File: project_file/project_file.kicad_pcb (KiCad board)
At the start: 2 copper layers, 44 x 84 mm, 76 parts, among them IC1 BMI055, J1 Power Module 1, J10 CAP & ADC IN, J11 SPI Port, J12 I2C A, J13 FMU PWM OUT, J14 PPM RC, J15 2908-05WB-MG, J16 RC, J17 SBUS, J18 IO/PWM out, J2 Power Module 2, J3 USB, J4 Telemetry 1, J5 Telemetry 2, J6 UART & I2C B, J7 CAN 1, J8 CAN 2, J9 GPS Module, U1 STM32F765IIKx, U10 TJA1051TK-3, U11 LT3080xDD, U12 LP5907MFX-3.3, U13 LP5907MFX-3.3, U3 IST8310, U4 ICM-20602, U5 ICM-20689, U6 MS5611-01BA, U8 STM32F103V8Tx, U9 TJA1051TK-3, Y1 ABM2-8.000MHZ-D4Y-T

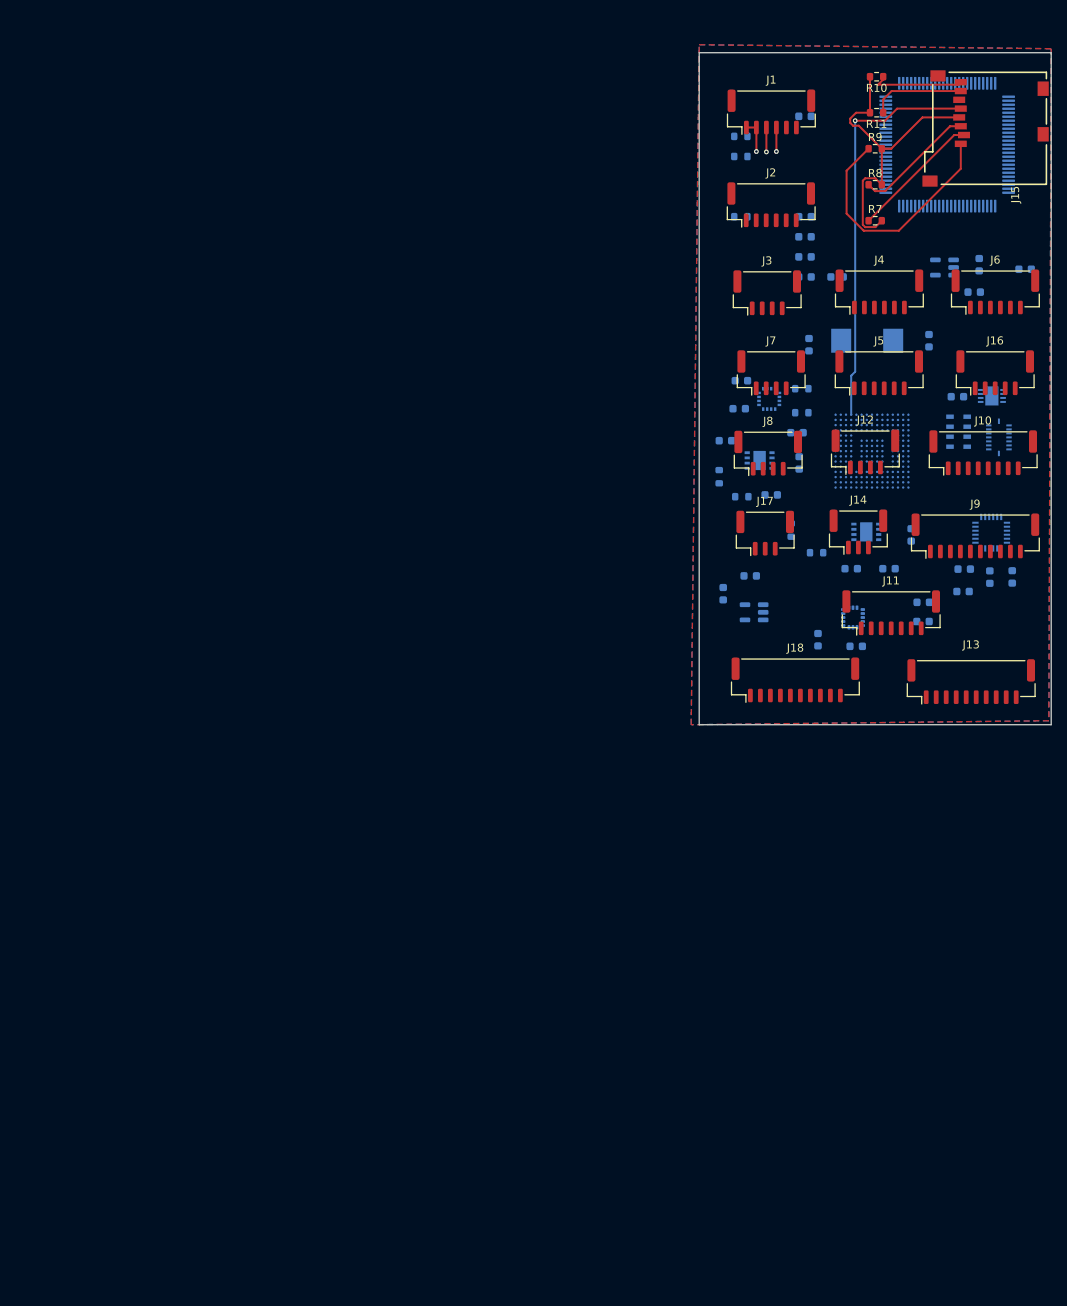
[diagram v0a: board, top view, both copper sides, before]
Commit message: CAN JST to pads, group pcb components tgt
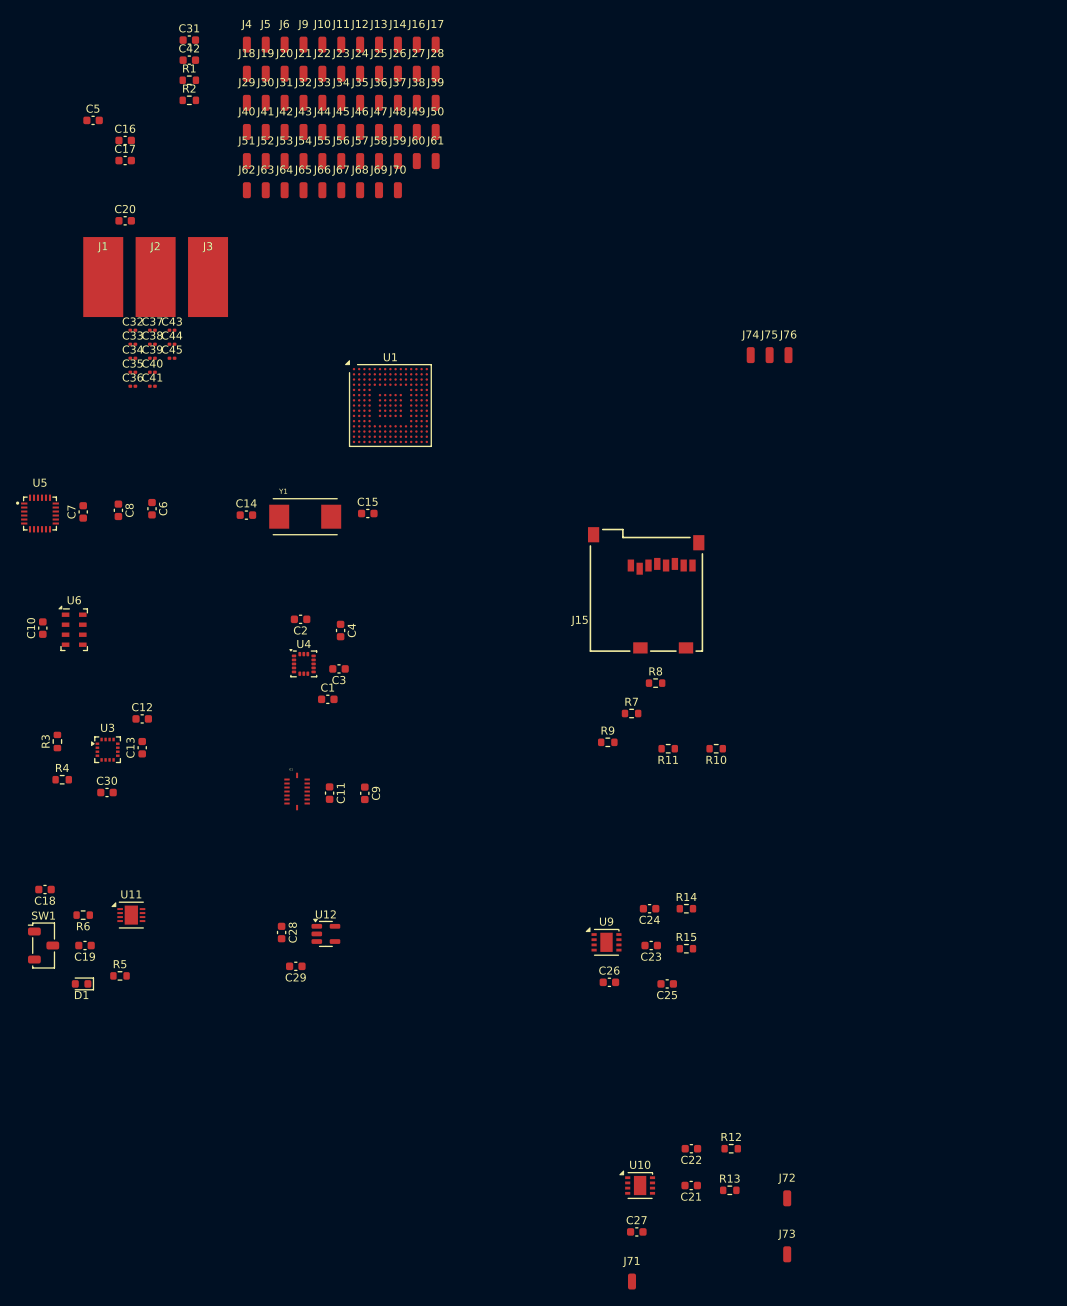
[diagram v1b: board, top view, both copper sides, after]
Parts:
- removed J7: CAN 1, Connector_JST:JST_GH_BM04B-GHS-TBT_1x04-1MP_P1.25mm_Vertical
- removed J8: CAN 2, Connector_JST:JST_GH_BM04B-GHS-TBT_1x04-1MP_P1.25mm_Vertical
- removed U13: LP5907MFX-3.3, Package_TO_SOT_SMD:SOT-23-5
- removed U8: STM32F103V8Tx, Package_QFP:LQFP-100_14x14mm_P0.5mm
- added C32: 100nf, Capacitor_SMD:C_0201_0603Metric, F.Cu at (36.2, 64.7)
- added C33: 100nf, Capacitor_SMD:C_0201_0603Metric, F.Cu at (36.2, 66.4)
- added C34: 100nf, Capacitor_SMD:C_0201_0603Metric, F.Cu at (36.2, 68.2)
- added C35: 100nf, Capacitor_SMD:C_0201_0603Metric, F.Cu at (36.2, 69.9)
- added C36: 100nf, Capacitor_SMD:C_0201_0603Metric, F.Cu at (36.2, 71.7)
- added C37: 100nf, Capacitor_SMD:C_0201_0603Metric, F.Cu at (38.7, 64.7)
- added C38: 100nf, Capacitor_SMD:C_0201_0603Metric, F.Cu at (38.7, 66.4)
- added C39: 100nf, Capacitor_SMD:C_0201_0603Metric, F.Cu at (38.7, 68.2)
- added C40: 100nf, Capacitor_SMD:C_0201_0603Metric, F.Cu at (38.7, 69.9)
- added C41: 100nf, Capacitor_SMD:C_0201_0603Metric, F.Cu at (38.7, 71.7)
- added C42: 0.1uF, Capacitor_SMD:C_0603_1608Metric, F.Cu at (43.3, 30.9)
- added C43: 100nf, Capacitor_SMD:C_0201_0603Metric, F.Cu at (41.1, 64.7)
- added C44: 100nf, Capacitor_SMD:C_0201_0603Metric, F.Cu at (41.1, 66.4)
- added C45: 100nf, Capacitor_SMD:C_0201_0603Metric, F.Cu at (41.1, 68.2)
- added D1: LED, LED_SMD:LED_0603_1608Metric, F.Cu at (29.8, 146.4)
- added J19: Conn_01x01_Socket, Connector_Wire:SolderWirePad_1x01_SMD_1x2mm, F.Cu at (52.8, 32.6)
- added J20: Conn_01x01_Socket, Connector_Wire:SolderWirePad_1x01_SMD_1x2mm, F.Cu at (55.2, 32.6)
- added J21: Conn_01x01_Socket, Connector_Wire:SolderWirePad_1x01_SMD_1x2mm, F.Cu at (57.5, 32.6)
- added J22: Conn_01x01_Socket, Connector_Wire:SolderWirePad_1x01_SMD_1x2mm, F.Cu at (59.9, 32.6)
- added J23: Conn_01x01_Socket, Connector_Wire:SolderWirePad_1x01_SMD_1x2mm, F.Cu at (62.3, 32.6)
- added J24: Conn_01x01_Socket, Connector_Wire:SolderWirePad_1x01_SMD_1x2mm, F.Cu at (64.6, 32.6)
- added J25: Conn_01x01_Socket, Connector_Wire:SolderWirePad_1x01_SMD_1x2mm, F.Cu at (67.0, 32.6)
- added J26: Conn_01x01_Socket, Connector_Wire:SolderWirePad_1x01_SMD_1x2mm, F.Cu at (69.3, 32.6)
- added J27: Conn_01x01_Socket, Connector_Wire:SolderWirePad_1x01_SMD_1x2mm, F.Cu at (71.7, 32.6)
- added J28: Conn_01x01_Socket, Connector_Wire:SolderWirePad_1x01_SMD_1x2mm, F.Cu at (74.1, 32.6)
- added J29: Conn_01x01_Socket, Connector_Wire:SolderWirePad_1x01_SMD_1x2mm, F.Cu at (50.5, 36.3)
- added J30: Conn_01x01_Socket, Connector_Wire:SolderWirePad_1x01_SMD_1x2mm, F.Cu at (52.8, 36.3)
- added J31: Conn_01x01_Socket, Connector_Wire:SolderWirePad_1x01_SMD_1x2mm, F.Cu at (55.2, 36.3)
- added J32: Conn_01x01_Socket, Connector_Wire:SolderWirePad_1x01_SMD_1x2mm, F.Cu at (57.5, 36.3)
- added J33: Conn_01x01_Socket, Connector_Wire:SolderWirePad_1x01_SMD_1x2mm, F.Cu at (59.9, 36.3)
- added J34: Conn_01x01_Socket, Connector_Wire:SolderWirePad_1x01_SMD_1x2mm, F.Cu at (62.3, 36.3)
- added J35: Conn_01x01_Socket, Connector_Wire:SolderWirePad_1x01_SMD_1x2mm, F.Cu at (64.6, 36.3)
- added J36: Conn_01x01_Socket, Connector_Wire:SolderWirePad_1x01_SMD_1x2mm, F.Cu at (67.0, 36.3)
- added J37: Conn_01x01_Socket, Connector_Wire:SolderWirePad_1x01_SMD_1x2mm, F.Cu at (69.3, 36.3)
- added J38: Conn_01x01_Socket, Connector_Wire:SolderWirePad_1x01_SMD_1x2mm, F.Cu at (71.7, 36.3)
- added J39: Conn_01x01_Socket, Connector_Wire:SolderWirePad_1x01_SMD_1x2mm, F.Cu at (74.1, 36.3)
- added J40: Conn_01x01_Socket, Connector_Wire:SolderWirePad_1x01_SMD_1x2mm, F.Cu at (50.5, 39.9)
- added J41: Conn_01x01_Socket, Connector_Wire:SolderWirePad_1x01_SMD_1x2mm, F.Cu at (52.8, 39.9)
- added J42: Conn_01x01_Socket, Connector_Wire:SolderWirePad_1x01_SMD_1x2mm, F.Cu at (55.2, 39.9)
- added J43: Conn_01x01_Socket, Connector_Wire:SolderWirePad_1x01_SMD_1x2mm, F.Cu at (57.5, 39.9)
- added J44: Conn_01x01_Socket, Connector_Wire:SolderWirePad_1x01_SMD_1x2mm, F.Cu at (59.9, 39.9)
- added J45: Conn_01x01_Socket, Connector_Wire:SolderWirePad_1x01_SMD_1x2mm, F.Cu at (62.3, 39.9)
- added J46: Conn_01x01_Socket, Connector_Wire:SolderWirePad_1x01_SMD_1x2mm, F.Cu at (64.6, 39.9)
- added J47: Conn_01x01_Socket, Connector_Wire:SolderWirePad_1x01_SMD_1x2mm, F.Cu at (67.0, 39.9)
- added J48: Conn_01x01_Socket, Connector_Wire:SolderWirePad_1x01_SMD_1x2mm, F.Cu at (69.3, 39.9)
- added J49: Conn_01x01_Socket, Connector_Wire:SolderWirePad_1x01_SMD_1x2mm, F.Cu at (71.7, 39.9)
- added J50: Conn_01x01_Socket, Connector_Wire:SolderWirePad_1x01_SMD_1x2mm, F.Cu at (74.1, 39.9)
- added J51: Conn_01x01_Socket, Connector_Wire:SolderWirePad_1x01_SMD_1x2mm, F.Cu at (50.5, 43.5)
- added J52: Conn_01x01_Socket, Connector_Wire:SolderWirePad_1x01_SMD_1x2mm, F.Cu at (52.8, 43.5)
- added J53: Conn_01x01_Socket, Connector_Wire:SolderWirePad_1x01_SMD_1x2mm, F.Cu at (55.2, 43.5)
- added J54: Conn_01x01_Socket, Connector_Wire:SolderWirePad_1x01_SMD_1x2mm, F.Cu at (57.5, 43.5)
- added J55: Conn_01x01_Socket, Connector_Wire:SolderWirePad_1x01_SMD_1x2mm, F.Cu at (59.9, 43.5)
- added J56: Conn_01x01_Socket, Connector_Wire:SolderWirePad_1x01_SMD_1x2mm, F.Cu at (62.3, 43.5)
- added J57: Conn_01x01_Socket, Connector_Wire:SolderWirePad_1x01_SMD_1x2mm, F.Cu at (64.6, 43.5)
- added J58: Conn_01x01_Socket, Connector_Wire:SolderWirePad_1x01_SMD_1x2mm, F.Cu at (67.0, 43.5)
- added J59: Conn_01x01_Socket, Connector_Wire:SolderWirePad_1x01_SMD_1x2mm, F.Cu at (69.3, 43.5)
- added J60: Conn_01x01_Socket, Connector_Wire:SolderWirePad_1x01_SMD_1x2mm, F.Cu at (71.7, 43.5)
- added J61: Conn_01x01_Socket, Connector_Wire:SolderWirePad_1x01_SMD_1x2mm, F.Cu at (74.1, 43.5)
- added J62: Conn_01x01_Socket, Connector_Wire:SolderWirePad_1x01_SMD_1x2mm, F.Cu at (50.5, 47.2)
- added J63: Conn_01x01_Socket, Connector_Wire:SolderWirePad_1x01_SMD_1x2mm, F.Cu at (52.8, 47.2)
- added J64: Conn_01x01_Socket, Connector_Wire:SolderWirePad_1x01_SMD_1x2mm, F.Cu at (55.2, 47.2)
- added J65: Conn_01x01_Socket, Connector_Wire:SolderWirePad_1x01_SMD_1x2mm, F.Cu at (57.5, 47.2)
- added J66: Conn_01x01_Socket, Connector_Wire:SolderWirePad_1x01_SMD_1x2mm, F.Cu at (59.9, 47.2)
- added J67: Conn_01x01_Socket, Connector_Wire:SolderWirePad_1x01_SMD_1x2mm, F.Cu at (62.3, 47.2)
- added J68: Conn_01x01_Socket, Connector_Wire:SolderWirePad_1x01_SMD_1x2mm, F.Cu at (64.6, 47.2)
- added J69: Conn_01x01_Socket, Connector_Wire:SolderWirePad_1x01_SMD_1x2mm, F.Cu at (67.0, 47.2)
- added J70: Conn_01x01_Socket, Connector_Wire:SolderWirePad_1x01_SMD_1x2mm, F.Cu at (69.3, 47.2)
- added J71: Conn_01x01_Socket, Connector_Wire:SolderWirePad_1x01_SMD_1x2mm, F.Cu at (98.6, 183.6)
- added J72: Conn_01x01_Socket, Connector_Wire:SolderWirePad_1x01_SMD_1x2mm, F.Cu at (118.0, 173.2)
- added J73: Conn_01x01_Socket, Connector_Wire:SolderWirePad_1x01_SMD_1x2mm, F.Cu at (118.0, 180.2)
- added J74: Conn_01x01_Socket, Connector_Wire:SolderWirePad_1x01_SMD_1x2mm, F.Cu at (113.4, 67.8)
- added J75: Conn_01x01_Socket, Connector_Wire:SolderWirePad_1x01_SMD_1x2mm, F.Cu at (115.8, 67.8)
- added J76: Conn_01x01_Socket, Connector_Wire:SolderWirePad_1x01_SMD_1x2mm, F.Cu at (118.2, 67.8)
- added R5: 300, Resistor_SMD:R_0603_1608Metric, F.Cu at (34.6, 145.4)
- added SW1: SW_Nidec_CAS-120A1, Button_Switch_SMD:Nidec_Copal_CAS-120A, F.Cu at (25.1, 141.6)
- C1, C10, C11, C12, C13, C14, C15, C16, C17, C18, C19, C2, C20, C21, C22, C23, C24, C25, C26, C27, C28, C29, C3, C4, C6, C7, C8, C9, IC1, R1, R12, R13, R14, R15, R2, R3, R4, R6, U1, U10, U11, U12, U3, U4, U5, U6, U9, Y1: moved to F.Cu
- C30, C31: value 1uf -> 0.1uF; moved to F.Cu
- C5: value 0.47uF -> 0.1uF; moved to F.Cu
- J1: value Power Module 1 -> Conn_01x01_Socket; footprint Connector_JST:JST_GH_BM06B-GHS-TBT_1x06-1MP_P1.25mm_Vertical -> Connector_Wire:SolderWirePad_1x01_SMD_5x10mm
- J10: value CAP & ADC IN -> Conn_01x01_Socket; footprint Connector_JST:JST_GH_BM08B-GHS-TBT_1x08-1MP_P1.25mm_Vertical -> Connector_Wire:SolderWirePad_1x01_SMD_1x2mm
- J11: value SPI Port -> Conn_01x01_Socket; footprint Connector_JST:JST_GH_BM07B-GHS-TBT_1x07-1MP_P1.25mm_Vertical -> Connector_Wire:SolderWirePad_1x01_SMD_1x2mm
- J12: value I2C A -> Conn_01x01_Socket; footprint Connector_JST:JST_GH_BM04B-GHS-TBT_1x04-1MP_P1.25mm_Vertical -> Connector_Wire:SolderWirePad_1x01_SMD_1x2mm
- J13: value FMU PWM OUT -> Conn_01x01_Socket; footprint Connector_JST:JST_EH_B10B-EH-A_1x10_P2.50mm_Vertical -> Connector_Wire:SolderWirePad_1x01_SMD_1x2mm
- J14: value PPM RC -> Conn_01x01_Socket; footprint Connector_JST:JST_GH_BM03B-GHS-TBT_1x03-1MP_P1.25mm_Vertical -> Connector_Wire:SolderWirePad_1x01_SMD_1x2mm
- J16: value RC -> Conn_01x01_Socket; footprint Connector_JST:JST_GH_BM05B-GHS-TBT_1x05-1MP_P1.25mm_Vertical -> Connector_Wire:SolderWirePad_1x01_SMD_1x2mm
- J17: value SBUS -> Conn_01x01_Socket; footprint Connector_JST:JST_GH_BM03B-GHS-TBT_1x03-1MP_P1.25mm_Vertical -> Connector_Wire:SolderWirePad_1x01_SMD_1x2mm
- J18: value IO/PWM out -> Conn_01x01_Socket; footprint Connector_JST:JST_GH_BM10B-GHS-TBT_1x10-1MP_P1.25mm_Vertical -> Connector_Wire:SolderWirePad_1x01_SMD_1x2mm
- J2: value Power Module 2 -> Conn_01x01_Socket; footprint Connector_JST:JST_GH_BM06B-GHS-TBT_1x06-1MP_P1.25mm_Vertical -> Connector_Wire:SolderWirePad_1x01_SMD_5x10mm
- J3: value USB -> Conn_01x01_Socket; footprint Connector_JST:JST_GH_BM04B-GHS-TBT_1x04-1MP_P1.25mm_Vertical -> Connector_Wire:SolderWirePad_1x01_SMD_5x10mm
- J4: value Telemetry 1 -> Conn_01x01_Socket; footprint Connector_JST:JST_GH_BM06B-GHS-TBT_1x06-1MP_P1.25mm_Vertical -> Connector_Wire:SolderWirePad_1x01_SMD_1x2mm
- J5: value Telemetry 2 -> Conn_01x01_Socket; footprint Connector_JST:JST_GH_BM06B-GHS-TBT_1x06-1MP_P1.25mm_Vertical -> Connector_Wire:SolderWirePad_1x01_SMD_1x2mm
- J6: value UART & I2C B -> Conn_01x01_Socket; footprint Connector_JST:JST_GH_BM06B-GHS-TBT_1x06-1MP_P1.25mm_Vertical -> Connector_Wire:SolderWirePad_1x01_SMD_1x2mm
- J9: value GPS Module -> Conn_01x01_Socket; footprint Connector_JST:JST_GH_BM10B-GHS-TBT_1x10-1MP_P1.25mm_Vertical -> Connector_Wire:SolderWirePad_1x01_SMD_1x2mm
- moved C5 125.8 mm to (31.2, 38.5), turned to 0 degrees
- moved U11 125.6 mm to (36.0, 137.8), turned to 0 degrees
- moved C18 123.6 mm to (25.2, 134.6)
- moved C19 122.8 mm to (30.2, 141.6)
- moved C28 120.7 mm to (54.8, 140.0)
- moved R6 119.9 mm to (30.0, 137.8)
- moved C29 119.6 mm to (56.6, 144.2), turned to 180 degrees
- moved U5 118.9 mm to (24.6, 87.6), turned to 0 degrees
- moved C10 117.9 mm to (24.9, 101.9), turned to 90 degrees
- moved C7 116.4 mm to (30.0, 87.4), turned to 90 degrees
- moved U12 113.7 mm to (60.3, 140.2), turned to 0 degrees
- moved U6 113.3 mm to (28.9, 102.1), turned to 0 degrees
- moved J13 108.3 mm to (67.0, 29.0)
- moved C8 106.1 mm to (34.4, 87.2), turned to -90 degrees
- moved J9 104.0 mm to (57.5, 29.0)
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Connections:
- C10 pad 2: VDD_sensors -> VDD_3V3
- C11 pad 1: VDDIO_sensors -> VDD_3V3
- C18 pad 1: BMS_22.2V -> Net-(U11-V_{CONTROL})
- C2 pad 2: VDD_sensors -> VDD_3V3
- C20 pad 1: Net-(J8-Pin_2) -> GND
- C25 pad 1: Net-(J7-Pin_2) -> GND
- C26 pad 2: /VDDIO -> VDD_3V3
- C27 pad 2: /VDDIO -> VDD_3V3
- C3 pad 1: VDDIO_sensors -> VDD_3V3
- C30 pad 1: BMS_22.2V -> VDD_3V3
- C31 pad 1: VCC_5V -> Net-(J31-Pin_1)
- C31 pad 2: GND -> VDD_3V3
- C4 pad 2: VDD_sensors -> VDD_3V3
- C6 pad 2: VDD_sensors -> VDD_3V3
- C7 pad 1: VDDIO_sensors -> VDD_3V3
- C8 pad 2: VDD_sensors -> VDD_3V3
- C9 pad 1: VDD_sensors -> VDD_3V3
- IC1 pad 11: VDDIO_sensors -> VDD_3V3
- IC1 pad 3: VDD_sensors -> VDD_3V3
- J1 pad 1: BMS_22.2V -> VDD_3V3
- J10 pad 1: VCC_5V -> BMS_22.2V
- J11 pad 1: VCC_5V -> BMS_22.2V
- J12 pad 1: GND -> BAT2_I
- J13 pad 1: unconnected-(J13-Pin_1-Pad1) -> BAT2_V
- J14 pad 1: VCC_5V -> VBUS
- J15 pad 4: VDD_ports -> VDD_3V3
- J16 pad 1: VCC_5V -> USB_DM
- J17 pad 1: unconnected-(J17-Pin_1-Pad1) -> USB_DP
- J18 pad 1: unconnected-(J18-Pin_1-Pad1) -> USART2_TX_TELEM1
- J2 pad 1: BMS_22.2V -> VCC_5V
- J3 pad 1: VBUS -> GND
- J4 pad 1: VCC_5V -> BMS_22.2V
- J5 pad 1: VCC_5V -> BMS_22.2V
- J6 pad 1: VCC_5V -> BAT1_I
- J9 pad 1: VCC_5V -> BAT1_V
- R1 pad 1: Net-(J16-Pin_3) -> Net-(J60-Pin_1)
- R10 pad 2: VDD_ports -> VDD_3V3
- R11 pad 2: VDD_ports -> VDD_3V3
- R12 pad 2: Net-(J8-Pin_2) -> GND
- R13 pad 2: Net-(J8-Pin_2) -> GND
- R14 pad 2: Net-(J7-Pin_2) -> GND
- R15 pad 2: Net-(J7-Pin_2) -> GND
- R3 pad 1: /VDD -> VDD_3V3
- R3 pad 2: /SDA_2 -> I2C3_SDA
- R4 pad 1: /VDD -> VDD_3V3
- R4 pad 2: /SCL_2 -> I2C3_SCL
- R7 pad 2: VDD_ports -> VDD_3V3
- R8 pad 2: VDD_ports -> VDD_3V3
- R9 pad 2: VDD_ports -> VDD_3V3
- U1 pad B10: SPI1_CS4_BMI055_ACC -> IO_CH5
- U1 pad B8: unconnected-(U1-PG12-PadB8) -> SPI1_SCK
- U1 pad B9: SPI1_SCK -> SPI1_CS4_BMI055_ACC
- U1 pad C10: unconnected-(U1-PG9-PadC10) -> IO_CH6
- U1 pad C13: unconnected-(U1-PI3-PadC13) -> IO_CH2
- U1 pad C14: unconnected-(U1-PI2-PadC14) -> IO_CH3
- U1 pad C2: unconnected-(U1-PI7-PadC2) -> RC_INPUT (aka PPM_IN)
- U1 pad C3: unconnected-(U1-PI6-PadC3) -> USART6_TX_TELEM3/(RC_INPUT)
- U1 pad C4: unconnected-(U1-PI5-PadC4) -> RSSI_IN
- U1 pad C5: VDD_sensors -> Net-(C45-Pad2)
- U1 pad C7: VDDIO_sensors -> Net-(C44-Pad2)
- U1 pad C9: VDD_ports -> Net-(C43-Pad2)
- U1 pad D14: unconnected-(U1-PI1-PadD14) -> IO_CH4
- U1 pad D2: unconnected-(U1-PI8-PadD2) -> FMU_CAP3
- U1 pad D3: CAN1_RX -> SPI5_CS1_EXTERNAL1
- U1 pad D4: SPI5_CS1_EXTERNAL1 -> IO_CH1
- U1 pad E14: unconnected-(U1-PI0-PadE14) -> SBUS_OUT
- U1 pad E3: SPI5_CS2_EXTERNAL1 -> CAN1_RX
- U1 pad E4: unconnected-(U1-PI11-PadE4) -> SPI5_CS2_EXTERNAL1
- U1 pad F3: VDD_3V3 -> Net-(C32-Pad2)
- U1 pad G13: VDD_3V3 -> Net-(C34-Pad2)
- U1 pad G3: VDD_3V3 -> Net-(C33-Pad2)
- U1 pad H14: unconnected-(U1-PG8-PadH14) -> IO_CH7
- U1 pad H4: unconnected-(U1-PH4-PadH4) -> ADC1_SPARE_1 (3.3V)
- U1 pad J12: VDD_3V3 -> Net-(C35-Pad2)
- U1 pad J13: VDD_3V3 -> Net-(C36-Pad2)
- U1 pad J14: unconnected-(U1-PG7-PadJ14) -> IO_CH8
- U1 pad J15: unconnected-(U1-PG6-PadJ15) -> VBUS
- U1 pad J4: unconnected-(U1-PH5-PadJ4) -> ADC1_SPARE_2 (6.6V)
- U1 pad K13: VDD_5V_RC_EN -> unconnected-(U1-PG5-PadK13)
- U1 pad K14: unconnected-(U1-PG4-PadK14) -> FMU_CAP1
- U1 pad K15: unconnected-(U1-PG3-PadK15) -> FMU_CAP2
- U1 pad K4: VDD_3V3 -> Net-(C37-Pad2)
- U1 pad L15: unconnected-(U1-PG2-PadL15) -> TIM1_CH1
- U1 pad M12: unconnected-(U1-PH8-PadM12) -> I2C3_SDA
- U1 pad M7: unconnected-(U1-PG1-PadM7) -> UART8_RX_PX4IO
- U1 pad N10: VDD_3V3 -> Net-(C40-Pad2)
- U1 pad N12: unconnected-(U1-PH7-PadN12) -> I2C3_SCL
- U1 pad N7: unconnected-(U1-PG0-PadN7) -> UART8_TX_PX4IO
- U1 pad N8: VDD_3V3 -> Net-(C38-Pad2)
- U1 pad N9: VDD_3V3 -> Net-(C39-Pad2)
- U1 pad R1: VDD_3V3 -> Net-(U1-VDDA)
- U10 pad 5: /VDDIO -> VDD_3V3
- U11 pad 5: BMS_22.2V -> Net-(U11-V_{CONTROL})
- U11 pad 7: BMS_22.2V -> Net-(U11-V_{CONTROL})
- U11 pad 8: BMS_22.2V -> Net-(U11-V_{CONTROL})
- U3 pad 1: /SCL_2 -> I2C3_SCL
- U3 pad 13: VDD_sensors -> VDD_3V3
- U3 pad 16: /SDA_2 -> I2C3_SDA
- U4 pad 1: VDDIO_sensors -> VDD_3V3
- U4 pad 16: VDD_sensors -> VDD_3V3
- U5 pad 13: VDD_sensors -> VDD_3V3
- U5 pad 8: VDDIO_sensors -> VDD_3V3
- U6 pad 1: VDD_sensors -> VDD_3V3
- U9 pad 5: /VDDIO -> VDD_3V3
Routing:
- net SDMMC1_CLK: track 50.8 -> 0.00 mm, vias 1 -> 0
- net VDD_ports: track 40.1 -> 0.00 mm
- net SDMMC1_D2: track 30.7 -> 0.00 mm
- net SDMMC1_D3: track 16.4 -> 0.00 mm
- net SDMMC1_CMD: track 15.2 -> 0.00 mm
- net SDMMC1_D0: track 11.8 -> 0.00 mm
- net SDMMC1_D1: track 11.7 -> 0.00 mm
- net BMS_22.2V: track 4.46 -> 0.00 mm, vias 1 -> 0
- net BAT1_V: track 3.21 -> 0.00 mm, vias 1 -> 0
- net BAT1_I: track 3.19 -> 0.00 mm, vias 1 -> 0
- removed copper zone on B.Cu, net GND
- removed copper zone on F.Cu, net GND
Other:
- board outline removed
- board text removed: "FMU PWM OUT"
- board text removed: "J13"
